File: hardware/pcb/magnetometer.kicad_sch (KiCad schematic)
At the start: 0 parts

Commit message: Update(hardware): Completed some schematics
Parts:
- added C10: 2.2u, symbol Device:C
- added C8, C9: 100n, symbol Device:C
- added IC1: BMM350, footprints:BGA9C40P3X3_128X128X54, symbol symbols:BMM350
- added R3: 10k, footprints:BGA9C40P3X3_128X128X54, symbol Device:R
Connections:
- new net: C10.1, IC1.C2 (CRST)
- new net: IC1.B2 (ADSEL), R3.1
- new net: C8.2, IC1.B3 (VDDIO)
- new net: C9.2, IC1.C1 (VDD)
- new net GNDPWR: C10.2, C8.1, C9.1, IC1.B1 (GND), IC1.C3 (BYPASS), R3.2
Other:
- note added: "Documentation available here"

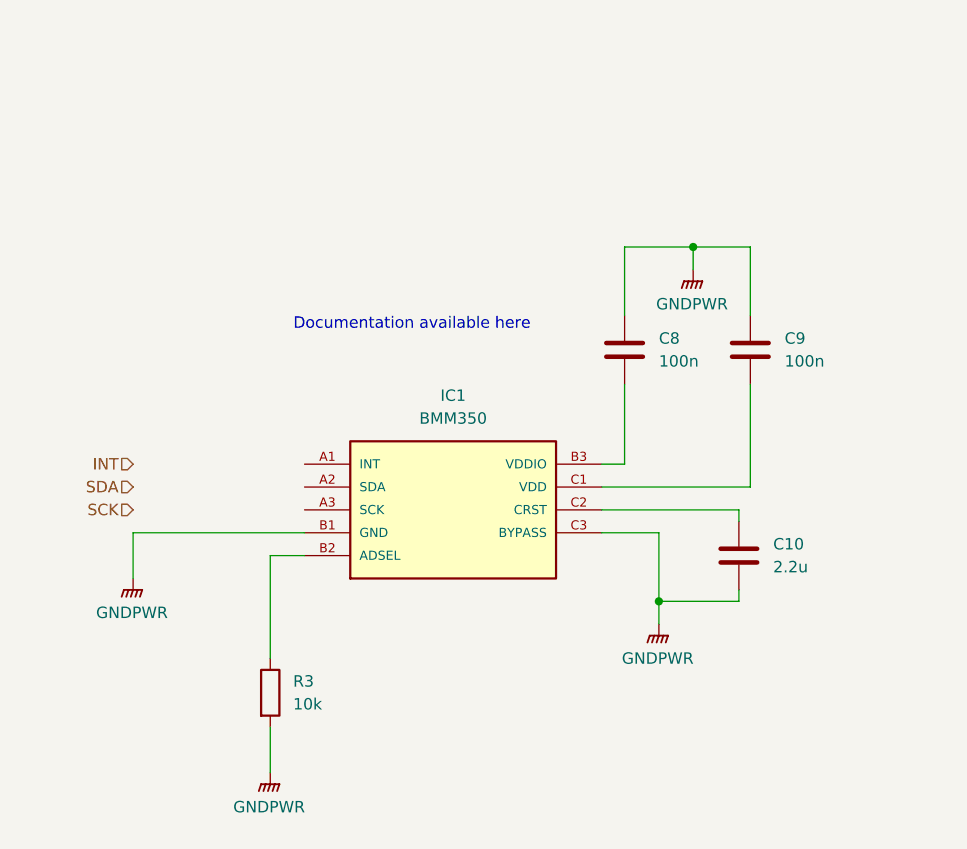
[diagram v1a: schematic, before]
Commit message: Changed GNDPWR to GND and changed GND to speciality GNDs
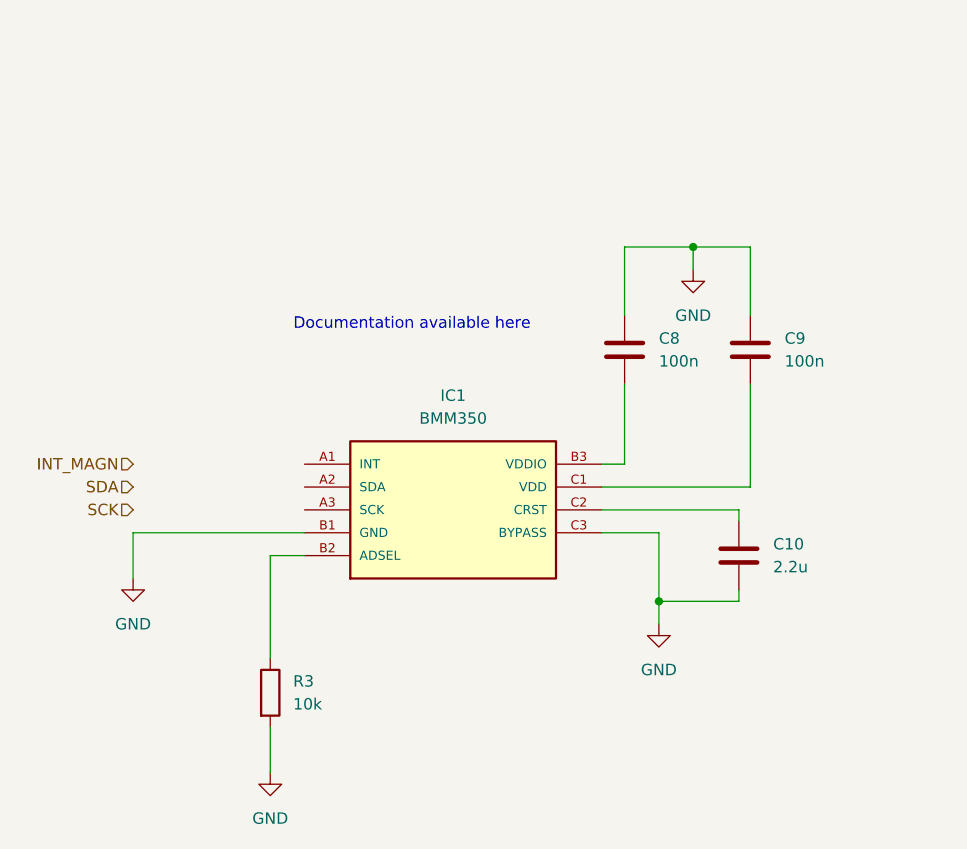
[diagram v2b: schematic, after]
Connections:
- net GNDPWR renamed GND
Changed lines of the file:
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@@
 		)
 	)
-	(hierarchical_label "INT"
+	(hierarchical_label "INT_MAGN"
 		(shape input)
 		(at 71.12 129.54 180)
@@
 			)
 			(justify right)
+		)
+	)
+	(symbol
+		(lib_id "power:GND")
+		(at 86.36 163.83 0)
+		(unit 1)
+		(body_style 1)
+		(exclude_from_sim no)
+		(in_bom yes)
+		(on_board yes)
+		(in_pos_files yes)
+		(dnp no)
+		(fields_autoplaced yes)
+		(property "Reference" "#PWR028"
+			(at 86.36 170.18 0)
+			(hide yes)
+			(show_name no)
+			(do_not_autoplace no)
+			(effects
+				(font
+					(size 1.27 1.27)
+				)
+			)
+		)
+		(property "Value" "GND"
+			(at 86.36 168.91 0)
+			(show_name no)
+			(do_not_autoplace no)
+			(effects
+				(font
+					(size 1.27 1.27)
+				)
+			)
+		)
+		(property "Footprint" ""
+			(at 86.36 163.83 0)
+			(hide yes)
+			(show_name no)
+			(do_not_autoplace no)
+			(effects
+				(font
+					(size 1.27 1.27)
+				)
+			)
+		)
+		(property "Datasheet" ""
+			(at 86.36 163.83 0)
+			(hide yes)
+			(show_name no)
+			(do_not_autoplace no)
+			(effects
+				(font
+					(size 1.27 1.27)
+				)
+			)
+		)
+		(property "Description" "Power symbol creates a global label with name \"GND\" , ground"
+			(at 86.36 163.83 0)
+			(hide yes)
+			(show_name no)
+			(do_not_autoplace no)
+			(effects
+				(font
+					(size 1.27 1.27)
+				)
+			)
+		)
+		(pin "1"
+		)
+		(instances
+			(project "test-circuits"
+				(path "/7b1b7b91-6618-446c-b915-39ecd9748633/ba1edd3c-e270-4599-b23e-fe027834271a"
+					(reference "#PWR028")
+					(unit 1)
+				)
+			)
 		)
 	)
@@
 	)
 	(symbol
-		(lib_id "power:GNDPWR")
-		(at 71.12 142.24 0)
-		(unit 1)
-		(body_style 1)
-		(exclude_from_sim no)
-		(in_bom yes)
-		(on_board yes)
-		(in_pos_files yes)
-		(dnp no)
-		(fields_autoplaced yes)
-		(property "Reference" "#PWR028"
-			(at 71.12 147.32 0)
-			(hide yes)
-			(show_name no)
-			(do_not_autoplace no)
-			(effects
-				(font
-					(size 1.27 1.27)
-				)
-			)
-		)
-		(property "Value" "GNDPWR"
-			(at 70.993 146.05 0)
-			(show_name no)
-			(do_not_autoplace no)
-			(effects
-				(font
-					(size 1.27 1.27)
-				)
-			)
-		)
-		(property "Footprint" ""
-			(at 71.12 143.51 0)
-			(hide yes)
-			(show_name no)
-			(do_not_autoplace no)
-			(effects
-				(font
-					(size 1.27 1.27)
-				)
-			)
-		)
-		(property "Datasheet" ""
-			(at 71.12 143.51 0)
-			(hide yes)
-			(show_name no)
-			(do_not_autoplace no)
-			(effects
-				(font
-					(size 1.27 1.27)
-				)
-			)
-		)
-		(property "Description" "Power symbol creates a global label with name \"GNDPWR\" , global ground"
-			(at 71.12 142.24 0)
-			(hide yes)
-			(show_name no)
-			(do_not_autoplace no)
-			(effects
-				(font
-					(size 1.27 1.27)
-				)
-			)
-		)
-		(pin "1"
-		)
-		(instances
-			(project "test-circuits"
-				(path "/7b1b7b91-6618-446c-b915-39ecd9748633/ba1edd3c-e270-4599-b23e-fe027834271a"
-					(reference "#PWR028")
-					(unit 1)
-				)
-			)
-		)
-	)
-	(symbol
-		(lib_id "power:GNDPWR")
+		(lib_id "power:GND")
 		(at 129.54 147.32 0)
 		(unit 1)
@@
 		(dnp no)
 		(fields_autoplaced yes)
-		(property "Reference" "#PWR031"
+		(property "Reference" "#PWR030"
+			(at 129.54 153.67 0)
+			(hide yes)
+			(show_name no)
+			(do_not_autoplace no)
+			(effects
+				(font
+					(size 1.27 1.27)
+				)
+			)
+		)
+		(property "Value" "GND"
 			(at 129.54 152.4 0)
-			(hide yes)
-			(show_name no)
-			(do_not_autoplace no)
-			(effects
-				(font
-					(size 1.27 1.27)
-				)
-			)
-		)
-		(property "Value" "GNDPWR"
-			(at 129.413 151.13 0)
 			(show_name no)
 			(do_not_autoplace no)
@@
 		)
 		(property "Footprint" ""
-			(at 129.54 148.59 0)
+			(at 129.54 147.32 0)
 			(hide yes)
 			(show_name no)
@@
 		)
 		(property "Datasheet" ""
-			(at 129.54 148.59 0)
-			(hide yes)
-			(show_name no)
-			(do_not_autoplace no)
-			(effects
-				(font
-					(size 1.27 1.27)
-				)
-			)
-		)
-		(property "Description" "Power symbol creates a global label with name \"GNDPWR\" , global ground"
+			(at 129.54 147.32 0)
+			(hide yes)
+			(show_name no)
+			(do_not_autoplace no)
+			(effects
+				(font
+					(size 1.27 1.27)
+				)
+			)
+		)
+		(property "Description" "Power symbol creates a global label with name \"GND\" , ground"
 			(at 129.54 147.32 0)
 			(hide yes)
@@
 			(project "test-circuits"
 				(path "/7b1b7b91-6618-446c-b915-39ecd9748633/ba1edd3c-e270-4599-b23e-fe027834271a"
-					(reference "#PWR031")
+					(reference "#PWR030")
 					(unit 1)
 				)
@@
 	)
 	(symbol
-		(lib_id "power:GNDPWR")
+		(lib_id "power:GND")
 		(at 133.35 107.95 0)
 		(unit 1)
@@
 		(dnp no)
 		(fields_autoplaced yes)
-		(property "Reference" "#PWR030"
+		(property "Reference" "#PWR029"
+			(at 133.35 114.3 0)
+			(hide yes)
+			(show_name no)
+			(do_not_autoplace no)
+			(effects
+				(font
+					(size 1.27 1.27)
+				)
+			)
+		)
+		(property "Value" "GND"
 			(at 133.35 113.03 0)
-			(hide yes)
-			(show_name no)
-			(do_not_autoplace no)
-			(effects
-				(font
-					(size 1.27 1.27)
-				)
-			)
-		)
-		(property "Value" "GNDPWR"
-			(at 133.223 111.76 0)
 			(show_name no)
 			(do_not_autoplace no)
@@
 		)
 		(property "Footprint" ""
-			(at 133.35 109.22 0)
+			(at 133.35 107.95 0)
 			(hide yes)
 			(show_name no)
@@
 		)
 		(property "Datasheet" ""
-			(at 133.35 109.22 0)
-			(hide yes)
-			(show_name no)
-			(do_not_autoplace no)
-			(effects
-				(font
-					(size 1.27 1.27)
-				)
-			)
-		)
-		(property "Description" "Power symbol creates a global label with name \"GNDPWR\" , global ground"
+			(at 133.35 107.95 0)
+			(hide yes)
+			(show_name no)
+			(do_not_autoplace no)
+			(effects
+				(font
+					(size 1.27 1.27)
+				)
+			)
+		)
+		(property "Description" "Power symbol creates a global label with name \"GND\" , ground"
 			(at 133.35 107.95 0)
 			(hide yes)
@@
 			(project "test-circuits"
 				(path "/7b1b7b91-6618-446c-b915-39ecd9748633/ba1edd3c-e270-4599-b23e-fe027834271a"
-					(reference "#PWR030")
+					(reference "#PWR029")
 					(unit 1)
 				)
@@
 	)
 	(symbol
+		(lib_id "power:GND")
+		(at 71.12 142.24 0)
+		(unit 1)
+		(body_style 1)
+		(exclude_from_sim no)
+		(in_bom yes)
+		(on_board yes)
+		(in_pos_files yes)
+		(dnp no)
+		(fields_autoplaced yes)
+		(property "Reference" "#PWR026"
+			(at 71.12 148.59 0)
+			(hide yes)
+			(show_name no)
+			(do_not_autoplace no)
+			(effects
+				(font
+					(size 1.27 1.27)
+				)
+			)
+		)
+		(property "Value" "GND"
+			(at 71.12 147.32 0)
+			(show_name no)
+			(do_not_autoplace no)
+			(effects
+				(font
+					(size 1.27 1.27)
+				)
+			)
+		)
+		(property "Footprint" ""
+			(at 71.12 142.24 0)
+			(hide yes)
+			(show_name no)
+			(do_not_autoplace no)
+			(effects
+				(font
+					(size 1.27 1.27)
+				)
+			)
+		)
+		(property "Datasheet" ""
+			(at 71.12 142.24 0)
+			(hide yes)
+			(show_name no)
+			(do_not_autoplace no)
+			(effects
+				(font
+					(size 1.27 1.27)
+				)
+			)
+		)
+		(property "Description" "Power symbol creates a global label with name \"GND\" , ground"
+			(at 71.12 142.24 0)
+			(hide yes)
+			(show_name no)
+			(do_not_autoplace no)
+			(effects
+				(font
+					(size 1.27 1.27)
+				)
+			)
+		)
+		(pin "1"
+		)
+		(instances
+			(project "test-circuits"
+				(path "/7b1b7b91-6618-446c-b915-39ecd9748633/ba1edd3c-e270-4599-b23e-fe027834271a"
+					(reference "#PWR026")
+					(unit 1)
+				)
+			)
+		)
+	)
+	(symbol
 		(lib_id "Device:C")
 		(at 139.7 116.84 0)
@@
 					(unit 1)
 				)
-			)
-		)
-	)
-	(symbol
-		(lib_id "power:GNDPWR")
-		(at 86.36 163.83 0)
-		(unit 1)
-		(body_style 1)
-		(exclude_from_sim no)
-		(in_bom yes)
-		(on_board yes)
-		(in_pos_files yes)
-		(dnp no)
-		(fields_autoplaced yes)
-		(property "Reference" "#PWR029"
-			(at 86.36 168.91 0)
-			(hide yes)
-			(show_name no)
-			(do_not_autoplace no)
-			(effects
-				(font
-					(size 1.27 1.27)
-				)
-			)
-		)
-		(property "Value" "GNDPWR"
-			(at 86.233 167.64 0)
-			(show_name no)
-			(do_not_autoplace no)
-			(effects
-				(font
-					(size 1.27 1.27)
-				)
-			)
-		)
-		(property "Footprint" ""
-			(at 86.36 165.1 0)
-			(hide yes)
-			(show_name no)
-			(do_not_autoplace no)
-			(effects
-				(font
-					(size 1.27 1.27)
-				)
-			)
-		)
-		(property "Datasheet" ""
-			(at 86.36 165.1 0)
-			(hide yes)
-			(show_name no)
-			(do_not_autoplace no)
-			(effects
-				(font
-					(size 1.27 1.27)
-				)
-			)
-		)
-		(property "Description" "Power symbol creates a global label with name \"GNDPWR\" , global ground"
-			(at 86.36 163.83 0)
-			(hide yes)
-			(show_name no)
-			(do_not_autoplace no)
-			(effects
-				(font
-					(size 1.27 1.27)
-				)
-			)
-		)
-		(pin "1"
-		)
-		(instances
-			(project "test-circuits"
-				(path "/7b1b7b91-6618-446c-b915-39ecd9748633/ba1edd3c-e270-4599-b23e-fe027834271a"
-					(reference "#PWR029")
-					(unit 1)
-				)

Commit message: Added USB-C to UART connectivity for debugging and flashing
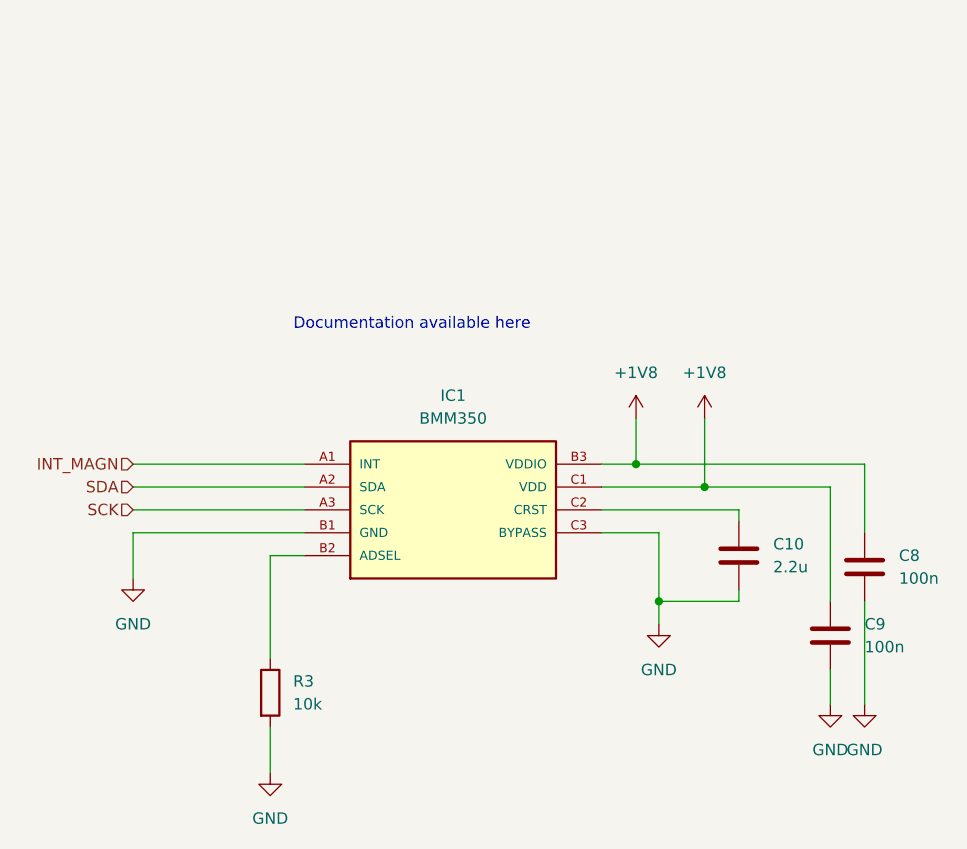
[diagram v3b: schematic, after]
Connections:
- net INT_MAGN: now also IC1.A1 (INT)
- net SCK: now also IC1.A3 (SCK)
- net SDA: now also IC1.A2 (SDA)
- net +1V8: now reaches C8.2, IC1.B3 (VDDIO)
- net +1V8: now also C9.2, IC1.C1 (VDD)
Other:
- moved on the sheet: C8, C9

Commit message: Progress on 3V3 circuit versions.
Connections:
- net +1V8 renamed +3V3
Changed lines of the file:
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@@
-	)
-	(symbol
-		(lib_id "power:+1V8")
-		(at 134.62 124.46 0)
-		(unit 1)
-		(body_style 1)
-		(exclude_from_sim no)
-		(in_bom yes)
-		(on_board yes)
-		(in_pos_files yes)
-		(dnp no)
-		(fields_autoplaced yes)
-		(property "Reference" "#PWR033"
-			(at 134.62 128.27 0)
-			(hide yes)
-			(show_name no)
-			(do_not_autoplace no)
-			(effects
-				(font
-					(size 1.27 1.27)
-				)
-			)
-		)
-		(property "Value" "+1V8"
-			(at 134.62 119.38 0)
-			(show_name no)
-			(do_not_autoplace no)
-			(effects
-				(font
-					(size 1.27 1.27)
-				)
-			)
-		)
-		(property "Footprint" ""
-			(at 134.62 124.46 0)
-			(hide yes)
-			(show_name no)
-			(do_not_autoplace no)
-			(effects
-				(font
-					(size 1.27 1.27)
-				)
-			)
-		)
-		(property "Datasheet" ""
-			(at 134.62 124.46 0)
-			(hide yes)
-			(show_name no)
-			(do_not_autoplace no)
-			(effects
-				(font
-					(size 1.27 1.27)
-				)
-			)
-		)
-		(property "Description" "Power symbol creates a global label with name \"+1V8\""
-			(at 134.62 124.46 0)
-			(hide yes)
-			(show_name no)
-			(do_not_autoplace no)
-			(effects
-				(font
-					(size 1.27 1.27)
-				)
-			)
-		)
-		(pin "1"
-		)
-		(instances
-			(project "test-circuits"
-				(path "/7b1b7b91-6618-446c-b915-39ecd9748633/ba1edd3c-e270-4599-b23e-fe027834271a"
-					(reference "#PWR033")
-					(unit 1)
-				)
-			)
-		)
 	)
 	(symbol
@@
 	)
 	(symbol
+		(lib_id "power:+3V3")
+		(at 134.62 124.46 0)
+		(unit 1)
+		(body_style 1)
+		(exclude_from_sim no)
+		(in_bom yes)
+		(on_board yes)
+		(in_pos_files yes)
+		(dnp no)
+		(fields_autoplaced yes)
+		(property "Reference" "#PWR033"
+			(at 134.62 128.27 0)
+			(hide yes)
+			(show_name no)
+			(do_not_autoplace no)
+			(effects
+				(font
+					(size 1.27 1.27)
+				)
+			)
+		)
+		(property "Value" "+3V3"
+			(at 134.62 119.38 0)
+			(show_name no)
+			(do_not_autoplace no)
+			(effects
+				(font
+					(size 1.27 1.27)
+				)
+			)
+		)
+		(property "Footprint" ""
+			(at 134.62 124.46 0)
+			(hide yes)
+			(show_name no)
+			(do_not_autoplace no)
+			(effects
+				(font
+					(size 1.27 1.27)
+				)
+			)
+		)
+		(property "Datasheet" ""
+			(at 134.62 124.46 0)
+			(hide yes)
+			(show_name no)
+			(do_not_autoplace no)
+			(effects
+				(font
+					(size 1.27 1.27)
+				)
+			)
+		)
+		(property "Description" "Power symbol creates a global label with name \"+3V3\""
+			(at 134.62 124.46 0)
+			(hide yes)
+			(show_name no)
+			(do_not_autoplace no)
+			(effects
+				(font
+					(size 1.27 1.27)
+				)
+			)
+		)
+		(pin "1"
+		)
+		(instances
+			(project "test-circuits"
+				(path "/7b1b7b91-6618-446c-b915-39ecd9748633/ba1edd3c-e270-4599-b23e-fe027834271a"
+					(reference "#PWR033")
+					(unit 1)
+				)
+			)
+		)
+	)
+	(symbol
 		(lib_id "symbols:BMM350")
 		(at 90.17 129.54 0)
@@
 	)
 	(symbol
-		(lib_id "power:+1V8")
-		(at 127 124.46 0)
-		(unit 1)
-		(body_style 1)
-		(exclude_from_sim no)
-		(in_bom yes)
-		(on_board yes)
-		(in_pos_files yes)
-		(dnp no)
-		(fields_autoplaced yes)
-		(property "Reference" "#PWR032"
-			(at 127 128.27 0)
-			(hide yes)
-			(show_name no)
-			(do_not_autoplace no)
-			(effects
-				(font
-					(size 1.27 1.27)
-				)
-			)
-		)
-		(property "Value" "+1V8"
-			(at 127 119.38 0)
-			(show_name no)
-			(do_not_autoplace no)
-			(effects
-				(font
-					(size 1.27 1.27)
-				)
-			)
-		)
-		(property "Footprint" ""
-			(at 127 124.46 0)
-			(hide yes)
-			(show_name no)
-			(do_not_autoplace no)
-			(effects
-				(font
-					(size 1.27 1.27)
-				)
-			)
-		)
-		(property "Datasheet" ""
-			(at 127 124.46 0)
-			(hide yes)
-			(show_name no)
-			(do_not_autoplace no)
-			(effects
-				(font
-					(size 1.27 1.27)
-				)
-			)
-		)
-		(property "Description" "Power symbol creates a global label with name \"+1V8\""
-			(at 127 124.46 0)
-			(hide yes)
-			(show_name no)
-			(do_not_autoplace no)
-			(effects
-				(font
-					(size 1.27 1.27)
-				)
-			)
-		)
-		(pin "1"
-		)
-		(instances
-			(project "test-circuits"
-				(path "/7b1b7b91-6618-446c-b915-39ecd9748633/ba1edd3c-e270-4599-b23e-fe027834271a"
-					(reference "#PWR032")
-					(unit 1)
-				)
-			)
-		)
-	)
-	(symbol
 		(lib_id "Device:C")
 		(at 152.4 140.97 180)
@@
 					(unit 1)
 				)
+			)
+		)
+	)
+	(symbol
+		(lib_id "power:+3V3")
+		(at 127 124.46 0)
+		(unit 1)
+		(body_style 1)
+		(exclude_from_sim no)
+		(in_bom yes)
+		(on_board yes)
+		(in_pos_files yes)
+		(dnp no)
+		(fields_autoplaced yes)
+		(property "Reference" "#PWR032"
+			(at 127 128.27 0)
+			(hide yes)
+			(show_name no)
+			(do_not_autoplace no)
+			(effects
+				(font
+					(size 1.27 1.27)
+				)
+			)
+		)
+		(property "Value" "+3V3"
+			(at 127 119.38 0)
+			(show_name no)
+			(do_not_autoplace no)
+			(effects
+				(font
+					(size 1.27 1.27)
+				)
+			)
+		)
+		(property "Footprint" ""
+			(at 127 124.46 0)
+			(hide yes)
+			(show_name no)
+			(do_not_autoplace no)
+			(effects
+				(font
+					(size 1.27 1.27)
+				)
+			)
+		)
+		(property "Datasheet" ""
+			(at 127 124.46 0)
+			(hide yes)
+			(show_name no)
+			(do_not_autoplace no)
+			(effects
+				(font
+					(size 1.27 1.27)
+				)
+			)
+		)
+		(property "Description" "Power symbol creates a global label with name \"+3V3\""
+			(at 127 124.46 0)
+			(hide yes)
+			(show_name no)
+			(do_not_autoplace no)
+			(effects
+				(font
+					(size 1.27 1.27)
+				)
+			)
+		)
+		(pin "1"
+		)
+		(instances
+			(project "test-circuits"
+				(path "/7b1b7b91-6618-446c-b915-39ecd9748633/ba1edd3c-e270-4599-b23e-fe027834271a"
+					(reference "#PWR032")
+					(unit 1)
+				)
